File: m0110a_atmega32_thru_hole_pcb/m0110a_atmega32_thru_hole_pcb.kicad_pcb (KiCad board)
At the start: 2 copper layers, 80 x 60 mm, 10 parts, among them J1 Conn_01x40_Pin, J2 ISP, J3 Serial Debug, U2 ATmega32A-M, Y1 ATS08A-E - 8MHz

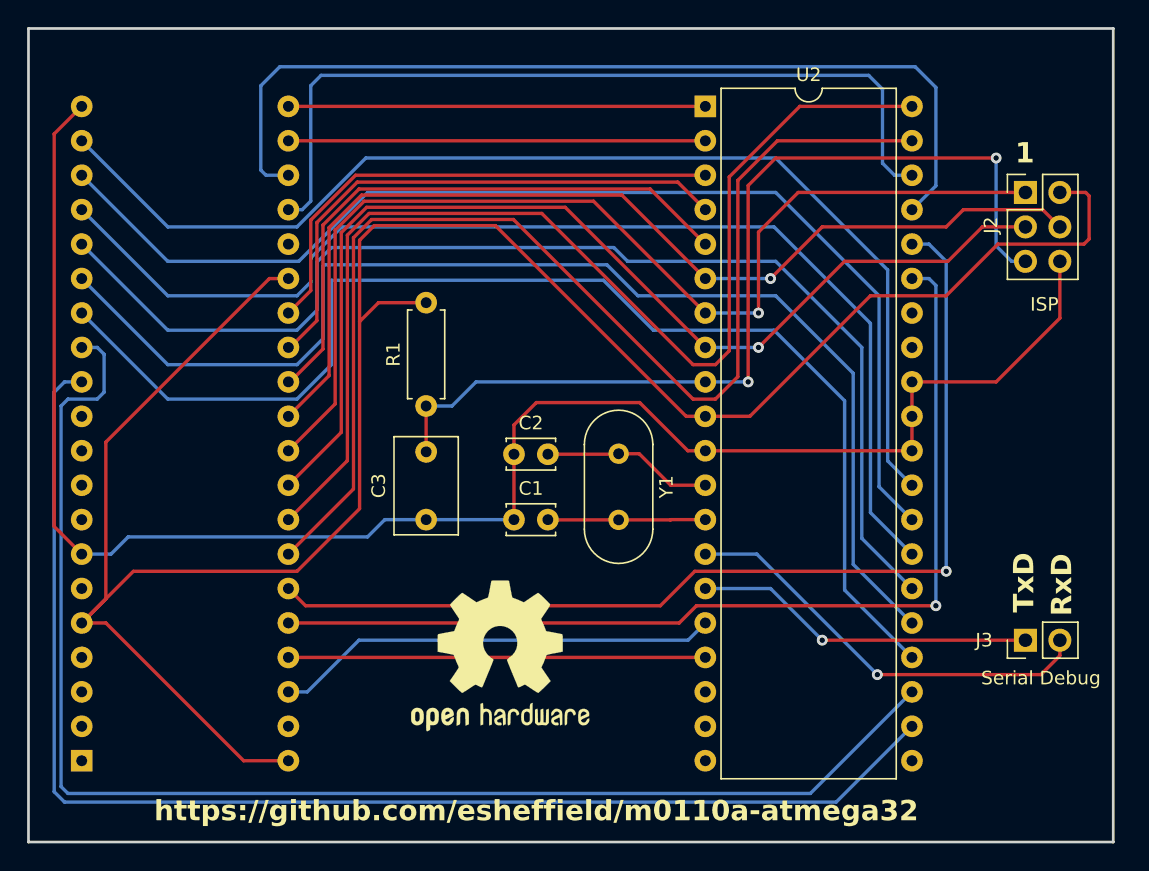
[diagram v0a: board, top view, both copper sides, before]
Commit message: Switched from external to internal clocking
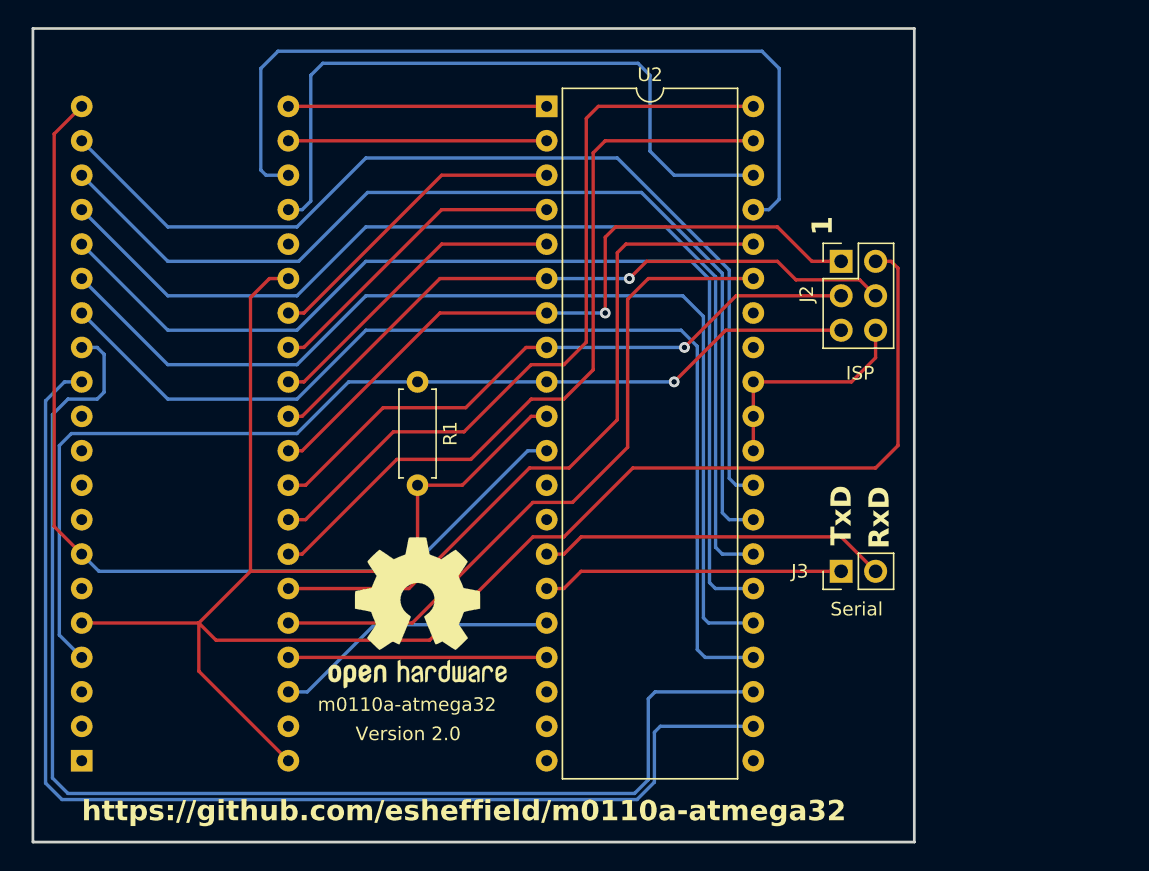
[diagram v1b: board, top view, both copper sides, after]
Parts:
- removed C1, C2: 22p, Capacitor_THT:C_Disc_D3.4mm_W2.1mm_P2.50mm
- removed C3: 1u, Capacitor_THT:C_Rect_L7.0mm_W4.5mm_P5.00mm
- removed Y1: ATS08A-E - 8MHz, Crystal:Crystal_HC49-U_Vertical
- J3: value Serial Debug -> Serial
- moved J2 14.5 mm to (149.6, 81.7)
- moved J3 14.5 mm to (149.6, 104.5)
- moved R1 13.5 mm to (118.4, 98.2), turned to 90 degrees
- moved U2 11.7 mm to (127.9, 70.2)
- moved REF** 6.87 mm to (118.4, 107.6)
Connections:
- J1 pad 4: unconnected-(J1-Pin_4-Pad4) -> RESET
- J2 pad 5: /RESET -> RESET
- R1 pad 2: /RESET -> RESET
- U2 pad 12: Net-(U2-XTAL2) -> unconnected-(U2-XTAL2-Pad12)
- U2 pad 13: Net-(U2-XTAL1) -> unconnected-(U2-XTAL1-Pad13)
- U2 pad 9: /RESET -> RESET
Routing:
- net RESET: track 0.00 -> 77.5 mm, vias 0 -> 1
- net /RESET: track 70.6 -> 0.00 mm, vias 2 -> 0
- net GNDREF: track 128.3 -> 90.1 mm
- net /ROW7: track 79.4 -> 46.6 mm
- net /ROW9: track 88.9 -> 56.3 mm
- net /ROW8: track 85.1 -> 56.6 mm
- net /ROW6: track 80.1 -> 51.9 mm
- net /ROW5: track 75.4 -> 49.1 mm
- net /OPT: track 76.0 -> 52.0 mm, vias 1 -> 0
- net /CMD: track 73.9 -> 51.2 mm, vias 1 -> 0
- net /ROW4: track 43.7 -> 23.3 mm
- net +5V: track 172.2 -> 153.3 mm
- net /ROW3: track 40.9 -> 23.3 mm
- net /ROW2: track 38.0 -> 23.3 mm
- net /COL5: track 90.8 -> 77.4 mm
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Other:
- board size 80 x 60 mm -> 65 x 60 mm
- board text added: "Version 2.0"
- board text added: "m0110a-atmega32"

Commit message: Removed unneeded resistor and ground connections
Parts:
- removed R1: 4k7, Resistor_THT:R_Axial_DIN0207_L6.3mm_D2.5mm_P7.62mm_Horizontal
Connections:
- U2 pad 30: GNDREF -> unconnected-(U2-AVCC-Pad30)
- U2 pad 32: GNDREF -> unconnected-(U2-AREF-Pad32)
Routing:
- net GNDREF: track 90.1 -> 161.6 mm
- net +5V: track 153.3 -> 191.7 mm
- net /LOCK: track 50.9 -> 56.5 mm
- net /KB_DATA: track 21.2 -> 26.5 mm
- net /COL3: track 77.4 -> 72.5 mm
- net /COL4: track 77.3 -> 72.9 mm
- net /COL5: track 77.4 -> 73.4 mm
- net /COL2: track 75.9 -> 72.3 mm
- net /SHIFT: track 60.8 -> 63.4 mm
- net /COL1: track 74.6 -> 72.0 mm
- net /COL0: track 73.3 -> 71.7 mm
- net /ROW8: track 56.6 -> 57.1 mm

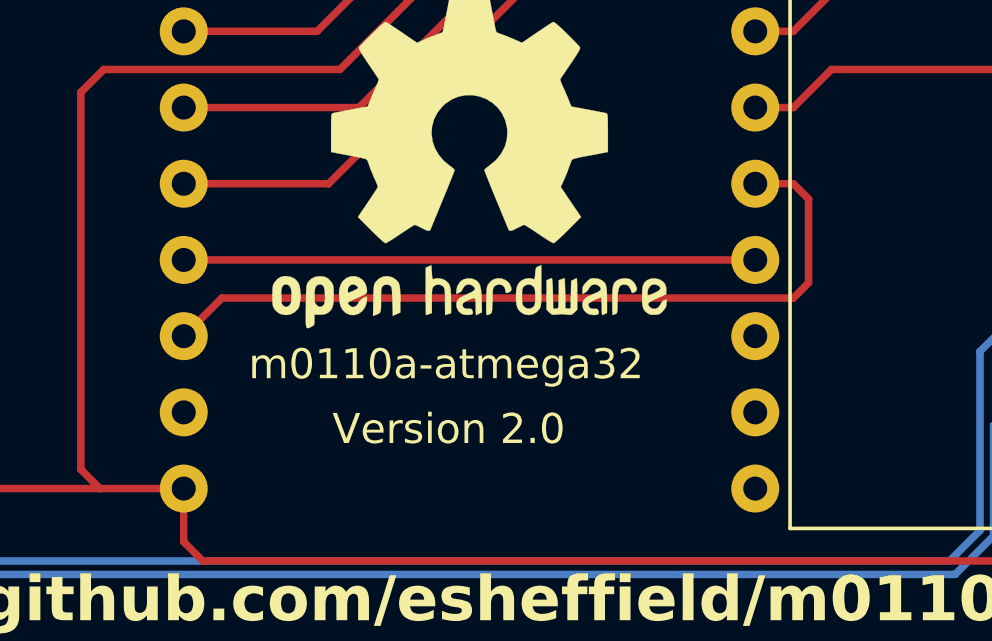
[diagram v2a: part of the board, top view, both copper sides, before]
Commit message: Swapped data and clk for easier layout. V 2.1
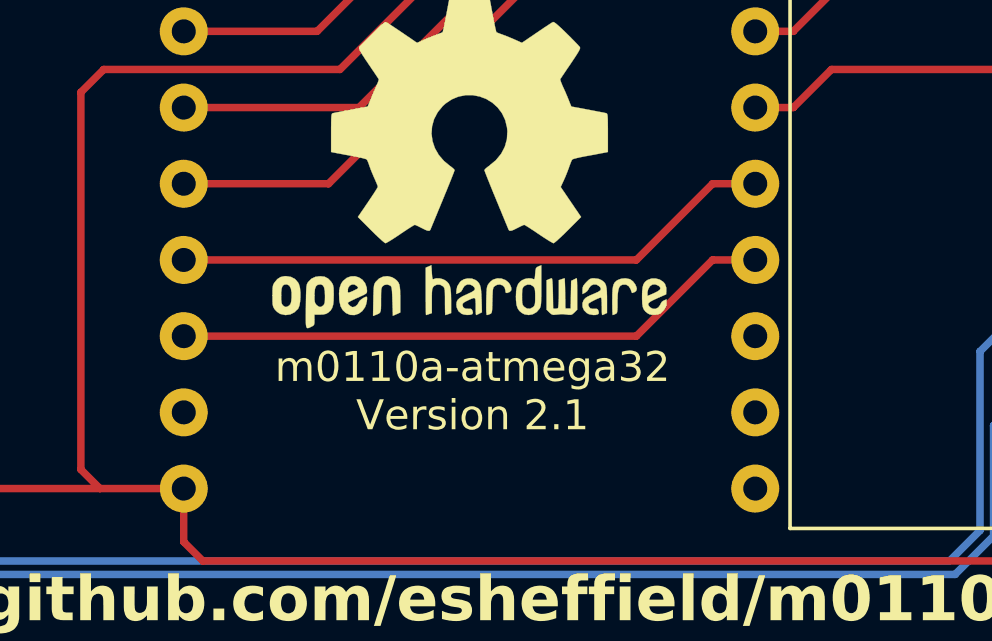
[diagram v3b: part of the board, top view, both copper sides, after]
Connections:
- U2 pad 16: /KB_DATA -> /KB_CLK
- U2 pad 17: /KB_CLK -> /KB_DATA
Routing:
- net /KB_DATA: track 26.5 -> 20.1 mm
- net /KB_CLK: track 19.0 -> 20.3 mm
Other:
- board text added: "m0110a-atmega32 Version 2.1"
- board text removed: "Version 2.0"
- board text removed: "m0110a-atmega32"
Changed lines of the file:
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@@
       (net 38 "/TXD") (pinfunction "PD1") (pintype "bidirectional"))
     (pad "16" thru_hole oval (at 0 38.1) (size 1.6 1.6) (drill 0.8) (layers "*.Cu" "*.Mask")
-      (net 36 "/KB_DATA") (pinfunction "PD2") (pintype "bidirectional"))
+      (net 35 "/KB_CLK") (pinfunction "PD2") (pintype "bidirectional"))
     (pad "17" thru_hole oval (at 0 40.64) (size 1.6 1.6) (drill 0.8) (layers "*.Cu" "*.Mask")
-      (net 35 "/KB_CLK") (pinfunction "PD3") (pintype "bidirectional"))
+      (net 36 "/KB_DATA") (pinfunction "PD3") (pintype "bidirectional"))
     (pad "18" thru_hole oval (at 0 43.18) (size 1.6 1.6) (drill 0.8) (layers "*.Cu" "*.Mask")
       (net 40 "unconnected-(U2-PD4-Pad18)") (pinfunction "PD4") (pintype "bidirectional+no_connect"))
@@
   (gr_rect (start 90 64.488) (end 155 124.488)
     (stroke (width 0.2) (type default)) (fill none) (layer "Edge.Cuts"))
-  (gr_text "Version 2.0" (at 113.792 117.094) (layer "F.SilkS")
-    (effects (font (size 1 1) (thickness 0.125)) (justify left bottom))
-  )
   (gr_text "1" (at 149.098 79.756 90) (layer "F.SilkS")
     (effects (font (size 1.5 1.5) (thickness 0.3) bold) (justify left bottom))
@@
     (effects (font (size 1.5 1.5) (thickness 0.3) bold) (justify left bottom))
   )
-  (gr_text "m0110a-atmega32" (at 110.998 114.935) (layer "F.SilkS")
-    (effects (font (size 1 1) (thickness 0.125)) (justify left bottom))
+  (gr_text "m0110a-atmega32\nVersion 2.1" (at 118.4656 116.6368) (layer "F.SilkS")
+    (effects (font (size 1 1) (thickness 0.125)) (justify bottom))
   )
   (gr_text "RxD" (at 153.289 102.87 90) (layer "F.SilkS")
@@
   (segment (start 113.665 108.331) (end 108.839 108.331) (width 0.25) (layer "F.Cu") (net 34))
   (segment (start 135.382 82.931) (end 133.858 84.455) (width 0.25) (layer "F.Cu") (net 34))
-  (segment (start 127.889 110.871) (end 108.839 110.871) (width 0.25) (layer "F.Cu") (net 35))
-  (segment (start 129.667 111.633) (end 129.667 108.839) (width 0.25) (layer "F.Cu") (net 36))
-  (segment (start 129.159 112.141) (end 129.667 111.633) (width 0.25) (layer "F.Cu") (net 36))
-  (segment (start 108.839 113.411) (end 110.109 112.141) (width 0.25) (layer "F.Cu") (net 36))
-  (segment (start 110.109 112.141) (end 129.159 112.141) (width 0.25) (layer "F.Cu") (net 36))
-  (segment (start 129.159 108.331) (end 127.889 108.331) (width 0.25) (layer "F.Cu") (net 36))
-  (segment (start 129.667 108.839) (end 129.159 108.331) (width 0.25) (layer "F.Cu") (net 36))
-  (segment (start 127.762 108.458) (end 127.889 108.331) (width 0.25) (layer "B.Cu") (net 36))
+  (segment (start 126.4666 108.331) (end 127.889 108.331) (width 0.25) (layer "F.Cu") (net 35))
+  (segment (start 123.9266 110.871) (end 126.4666 108.331) (width 0.25) (layer "F.Cu") (net 35))
+  (segment (start 108.839 110.871) (end 123.9266 110.871) (width 0.25) (layer "F.Cu") (net 35))
+  (segment (start 127.762 108.458) (end 127.889 108.331) (width 0.25) (layer "B.Cu") (net 35))
+  (segment (start 126.4666 110.871) (end 123.9266 113.411) (width 0.25) (layer "F.Cu") (net 36))
+  (segment (start 123.9266 113.411) (end 108.839 113.411) (width 0.25) (layer "F.Cu") (net 36))
+  (segment (start 127.889 110.871) (end 126.4666 110.871) (width 0.25) (layer "F.Cu") (net 36))
   (segment (start 130.429 104.521) (end 149.606 104.521) (width 0.25) (layer "F.Cu") (net 38))
   (segment (start 127.889 105.791) (end 129.159 105.791) (width 0.25) (layer "F.Cu") (net 38))

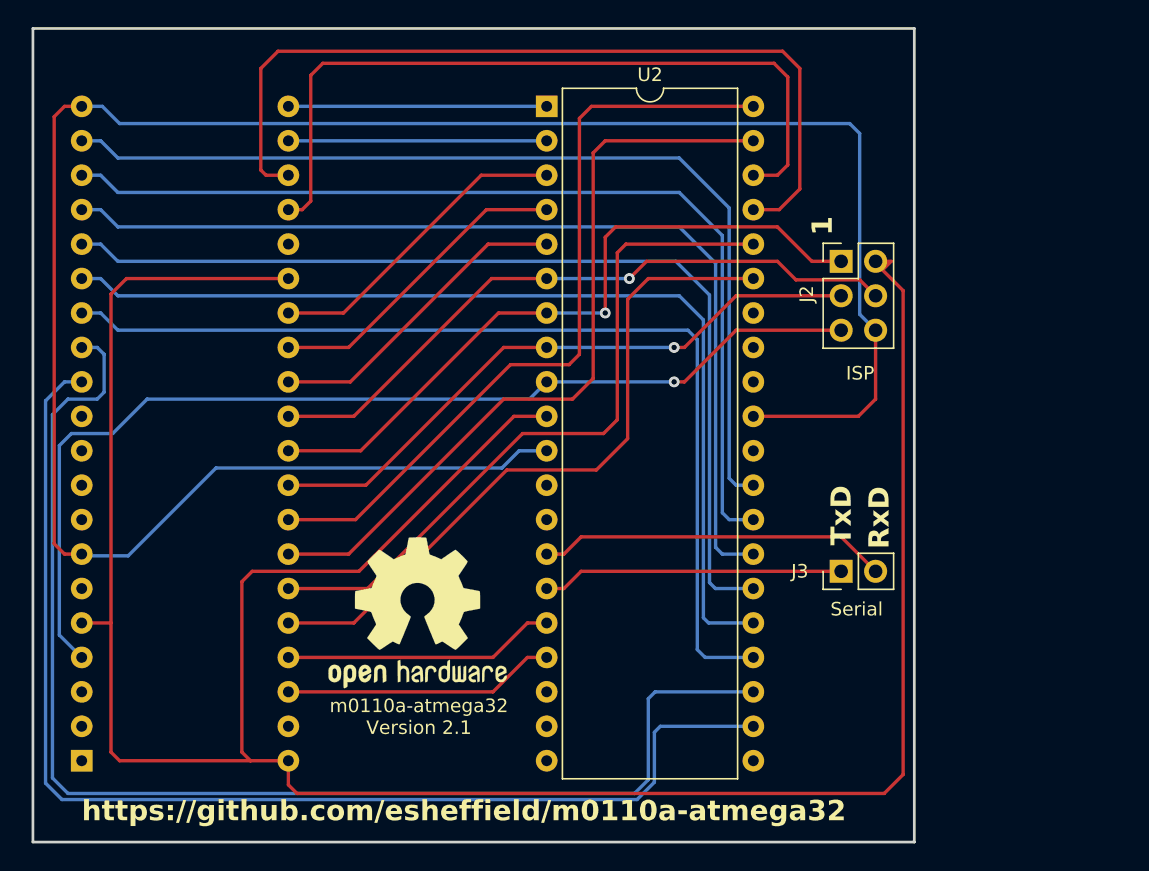
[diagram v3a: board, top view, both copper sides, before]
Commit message: Added gerbers (PCBWay rules)
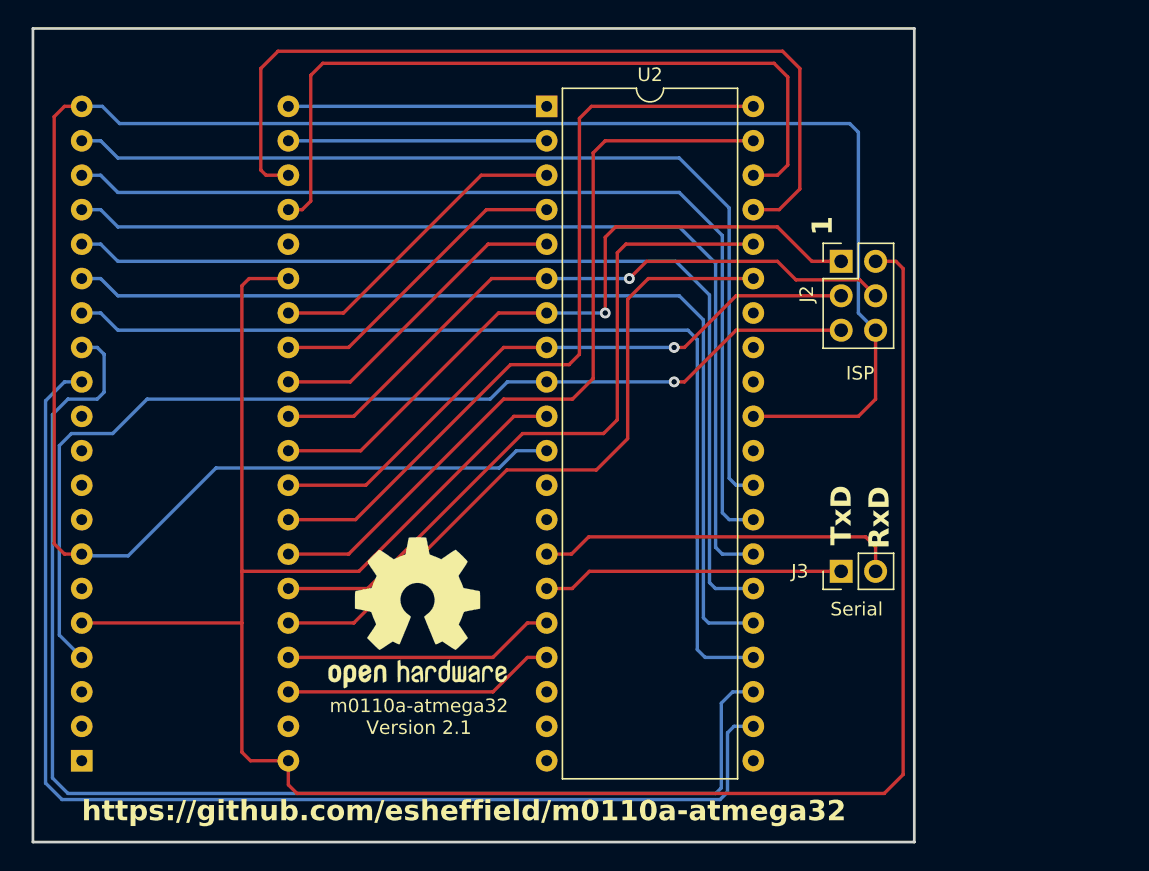
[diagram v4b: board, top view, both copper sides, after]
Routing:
- net +5V: track 191.7 -> 168.3 mm
- net /RXD: track 25.8 -> 26.9 mm

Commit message: Updated PCBs
- Increased hole size on 40 pin connector to accomodate standard pin headers
- Moved ISP connector on SMD board to clear support under spacebar
- Improved labeling on thru-hole board for ISP connector
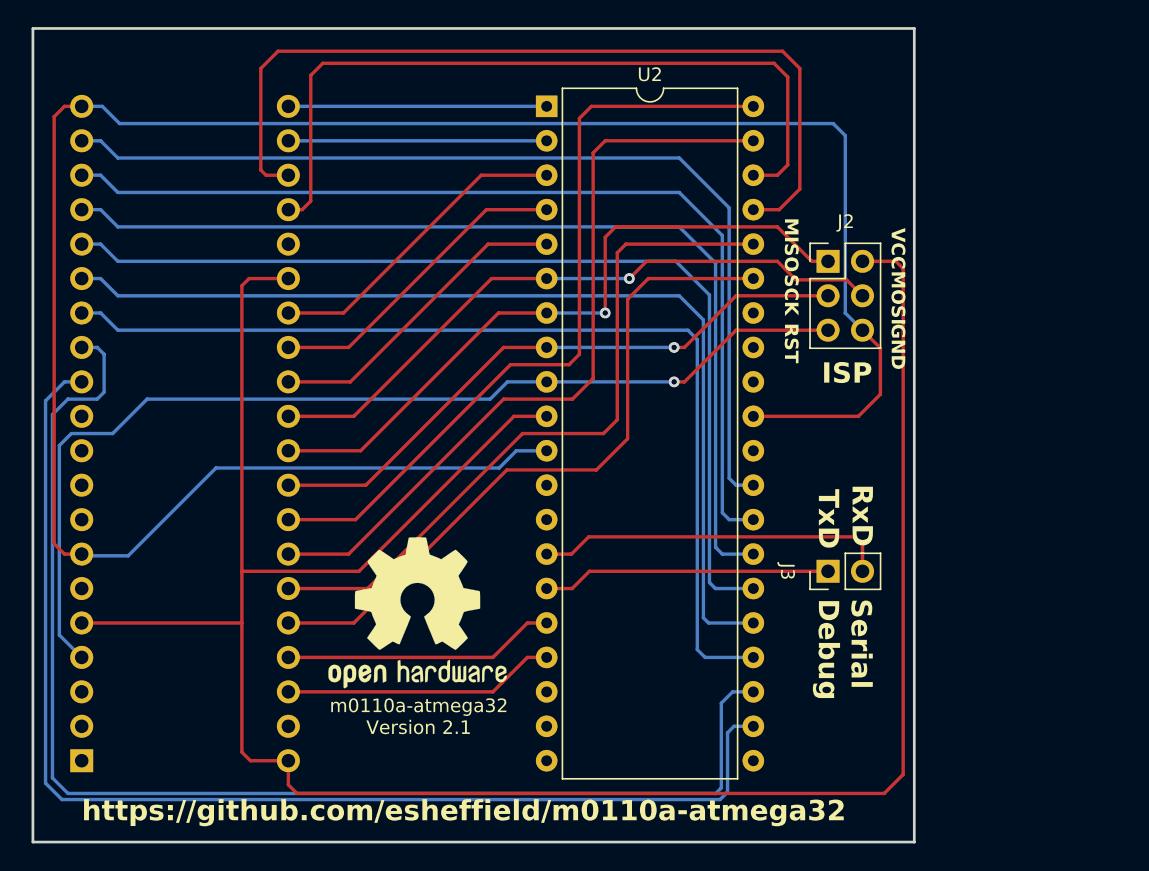
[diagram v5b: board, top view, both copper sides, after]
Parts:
- moved J2 0.97 mm to (148.6, 81.7)
- moved J3 0.97 mm to (148.6, 104.5)
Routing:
- net /ROW5: track 49.1 -> 48.1 mm
- net RESET: track 77.5 -> 76.5 mm
- net /TXD: track 22.2 -> 21.3 mm
- net /ROW7: track 46.6 -> 45.6 mm
- net /ROW6: track 51.9 -> 51.0 mm
- net +5V: track 168.3 -> 169.2 mm
- net /RXD: track 26.9 -> 26.0 mm
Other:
- board text added: "GND"
- board text added: "MISO"
- board text added: "MOSI"
- board text added: "RST"
- board text added: "SCK"
- board text added: "Serial Debug"
- board text added: "VCC"
- board text removed: "1"
